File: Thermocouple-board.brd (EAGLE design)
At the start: 76.2 x 78.7 mm, 82 parts, among them J1 RJ45, J10 1X2-3.5MM, J11 1X2-3.5MM, J12 1X2-3.5MM, J13 1X2-3.5MM, J2 RJ45, J3 1981584-1, J4 2.1MMJACKTHM, J5 ST-LINK, J6 HEADER-1X3, J7 UART, SW1 PUSHBUTTON, SW2 PUSHBUTTON, U1 STM32F042K4, U10 MAX31855, U11 MAX31855, U12 MAX31855, U13 MAX31855, U20 EEPROM-I2C, U21 EEPROM-I2C, U30 ST3485, U31 ST3485, U40 LP298XS, Y1 8MHz

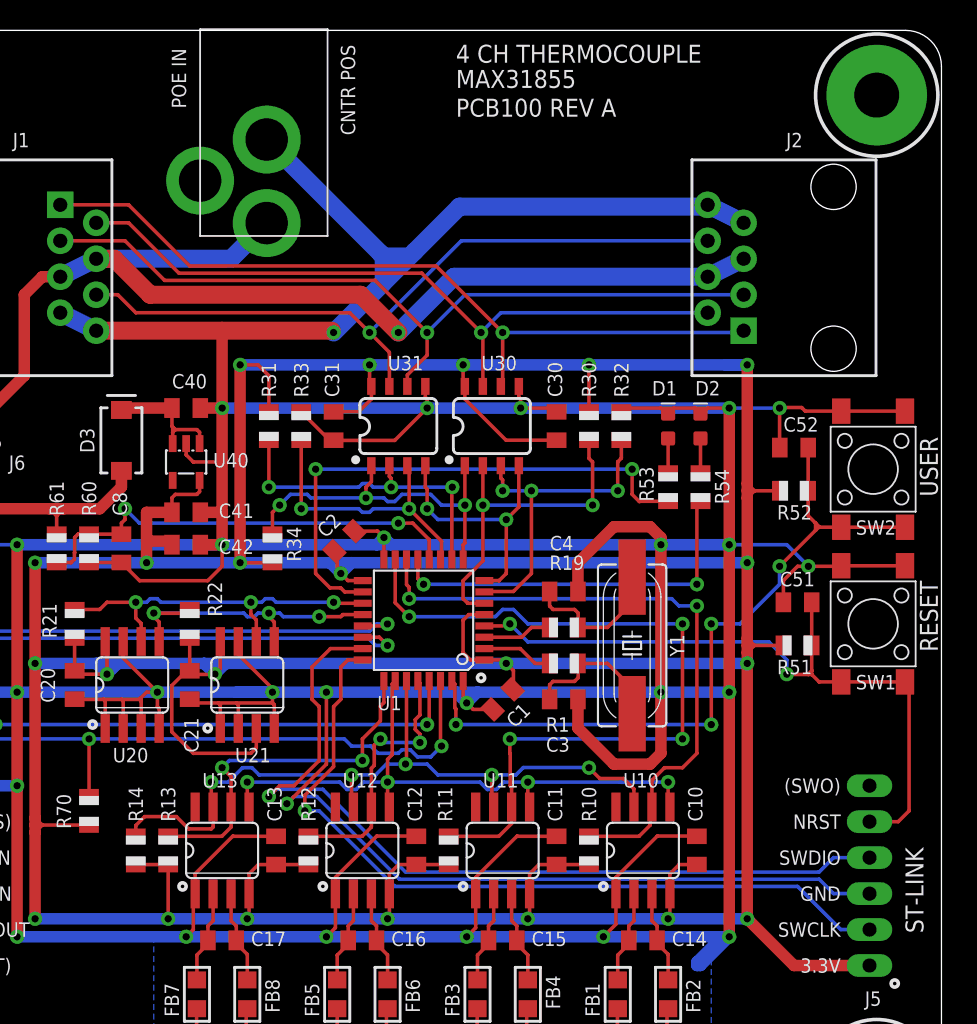
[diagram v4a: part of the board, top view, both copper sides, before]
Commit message: Fix pushbutton and SO08. Start of efuse.
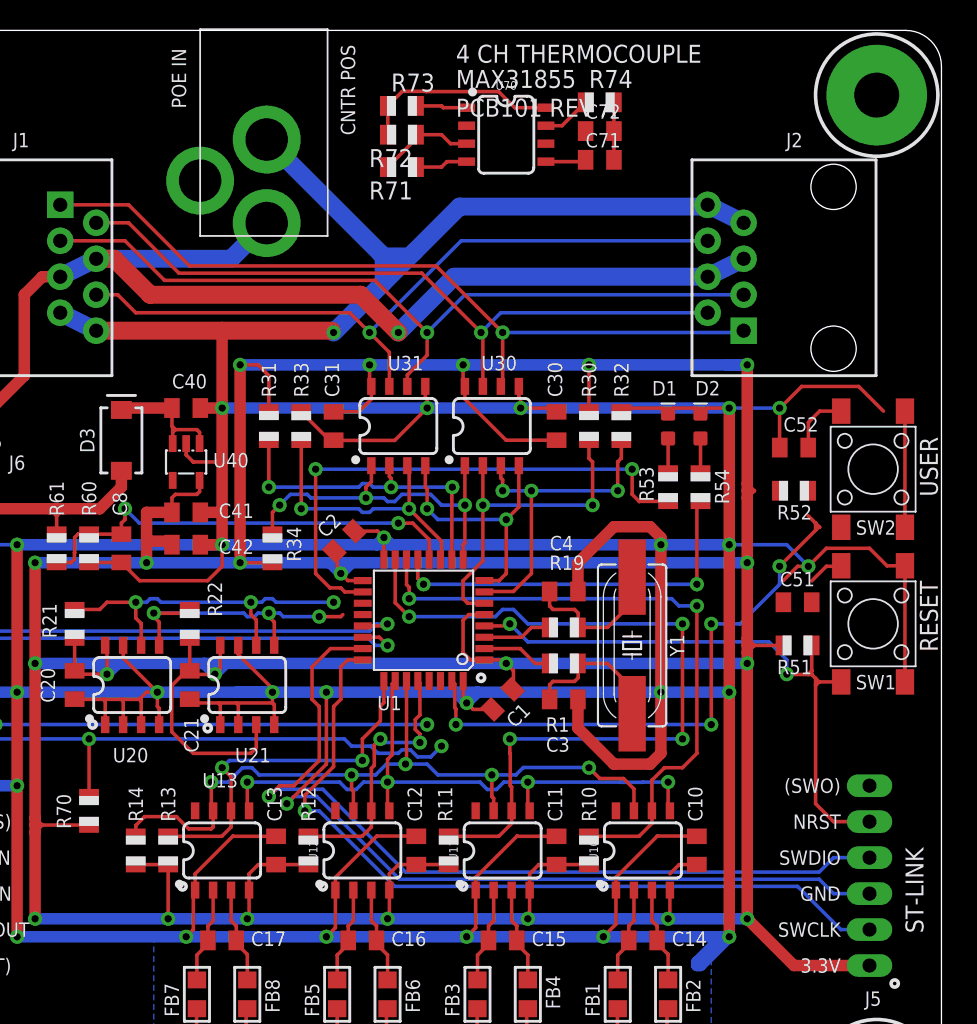
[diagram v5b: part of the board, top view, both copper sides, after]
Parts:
- added C71, C72: 10pF, adafruit:C0805K
- added R71, R72, R73, R74: 10K, adafruit:R0805
- added U70: TPS25921, Thermocouple-board:SO08
- U10, U11, U12, U13: device adafruit:SO08 -> Thermocouple-board:SO08
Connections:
- new net N$23: R71.2, R72.1, U70.3
- new net N$24: R72.2, R73.1, U70.8
- new net N$27: R74.1, U70.7
- new net N$28: C72.1, U70.2
- new net PWR_SRC: J4.TIP, R71.1, U70.4
- net +3V3: now also C52.1, SW2.1, SW2.2; no longer R52.1
- net BTN_USER: now also C52.2, R52.1, SW2.3; no longer C52.1, R52.2, SW2.2
- net GND: now also C71.2, C72.2, R52.2, R73.2, R74.2, SW1.2, U70.1; no longer C52.2, SW1.3, SW2.1, SW2.3
- net I2C_SCL: now also U1.29; no longer U1.19
- net I2C_SDA: now also U1.30; no longer U1.20
- net NRST: now also SW1.3; no longer SW1.2
- net POE_PWR: now also C71.1, U70.5; no longer J4.TIP
- net UART1_RX: now also U1.20; no longer U1.30
- net UART1_TX: now also U1.19; no longer U1.29
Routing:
- net N$24: track 0.00 -> 14.1 mm
- net GND: track 630.1 -> 642.8 mm
- net N$23: track 0.00 -> 6.94 mm
- net BTN_USER: track 52.1 -> 45.6 mm
- net +3V3: track 407.6 -> 412.8 mm
- net UART1_RX: track 55.9 -> 51.4 mm
- net NRST: track 50.0 -> 46.0 mm
- net PWR_SRC: track 0.00 -> 3.72 mm
- net N$27: track 0.00 -> 3.49 mm
- net UART1_TX: track 51.2 -> 48.3 mm
- net POE_PWR: track 82.2 -> 85.1 mm
- net I2C_SCL: track 26.9 -> 25.4 mm
- net I2C_SDA: track 22.1 -> 21.3 mm
- net SPI_MISO: track 54.1 -> 54.9 mm
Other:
- board text added: "PCB101 REV A"
- board text removed: "PCB100 REV A"

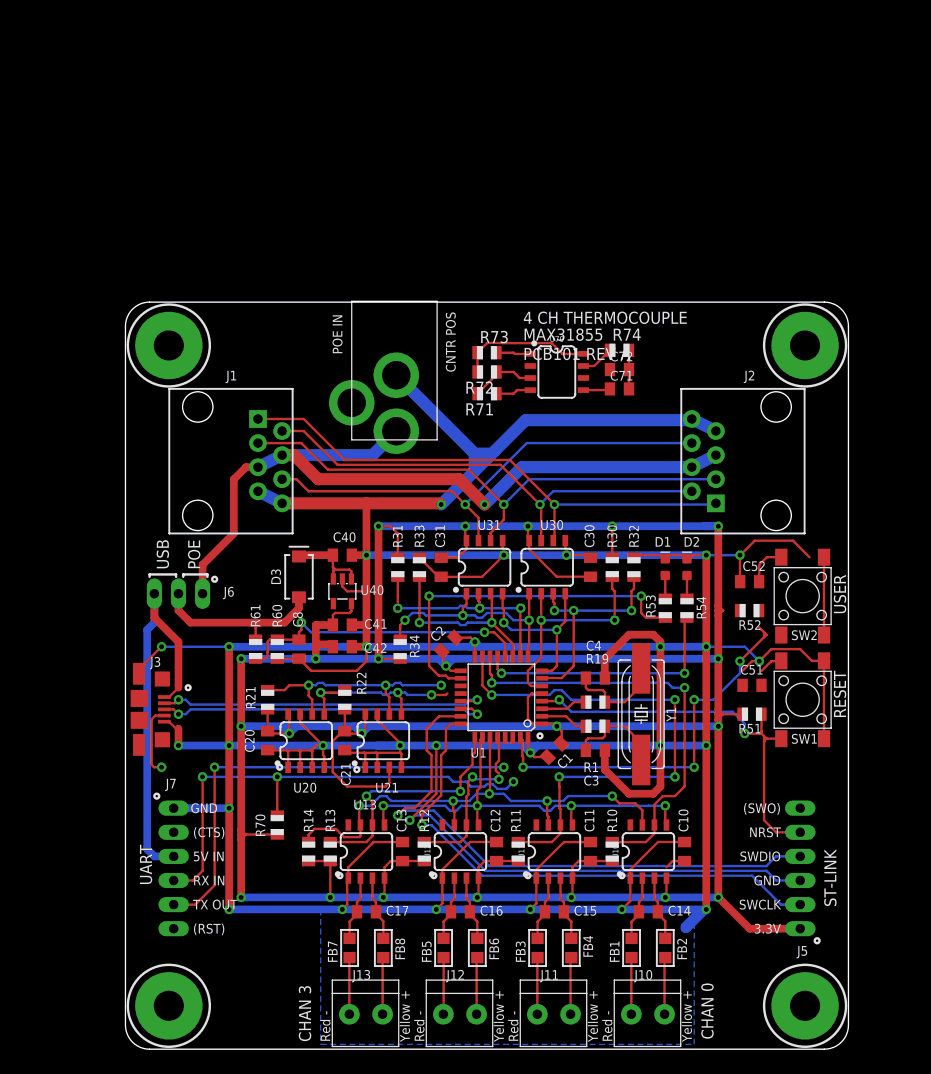
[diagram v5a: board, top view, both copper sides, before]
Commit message: RJ-45 rework routing WIP
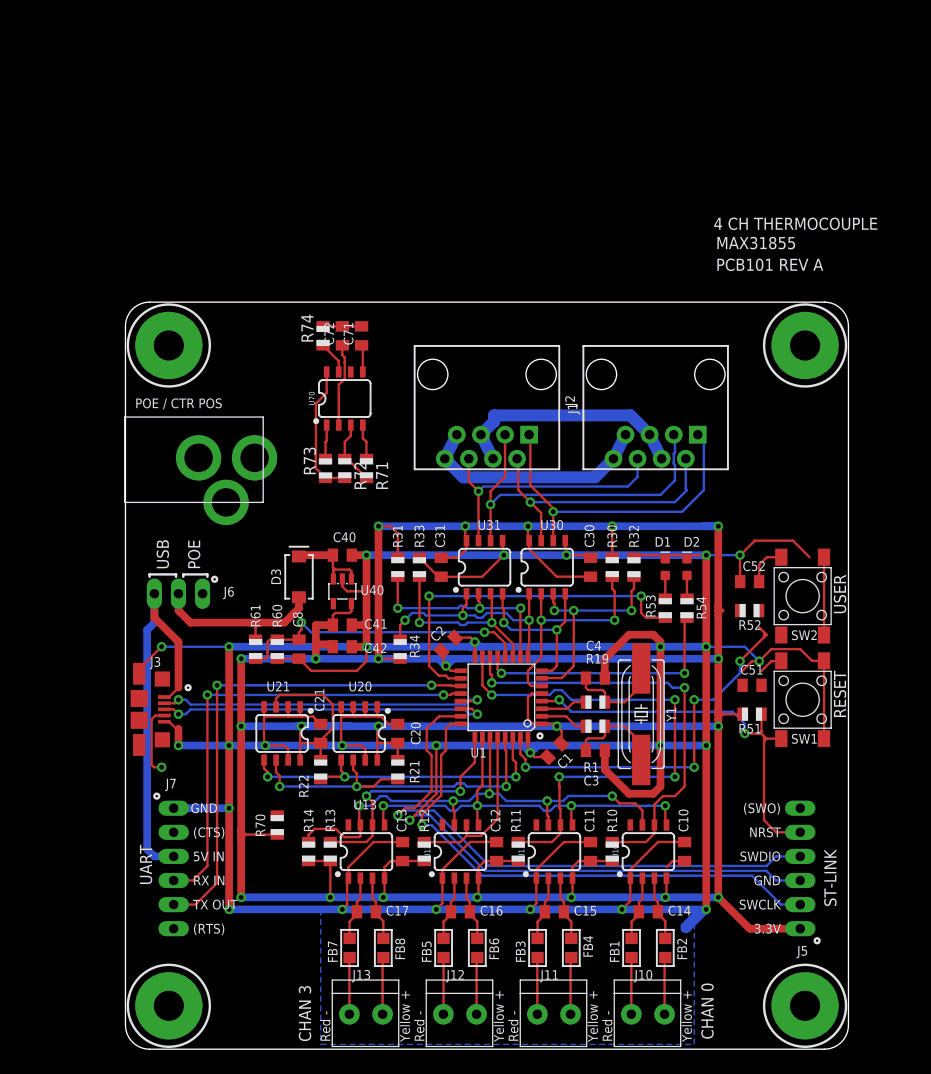
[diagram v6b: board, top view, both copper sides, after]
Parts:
- U1: value STM32F042K4 -> STM32F042K6
- moved J1 31.8 mm to (38.1, 71.1), turned to 180 degrees
- moved R74 31.3 mm to (20.8, 75.2), turned to 90 degrees
- moved C72 29.4 mm to (22.9, 75.2), turned to 90 degrees
- moved C71 27.7 mm to (24.9, 75.2), turned to 90 degrees
- moved J4 27.0 mm to (4.32, 62.2), turned to 90 degrees
- moved U70 22.5 mm to (23.1, 68.6), turned to 0 degrees
- moved R73 20.9 mm to (21.1, 61.2), turned to 90 degrees
- moved R72 18.1 mm to (23.1, 61.2), turned to 270 degrees
- moved J2 15.6 mm to (55.9, 71.1), turned to 180 degrees
- moved R21 15.6 mm to (28.7, 29.5), turned to 270 degrees
- moved R71 14.9 mm to (25.4, 61.2), turned to 270 degrees
- moved C20 13.7 mm to (28.7, 33.3), turned to 90 degrees
- moved U21 10.7 mm to (16.5, 33.3), turned to 180 degrees
- moved R22 7.79 mm to (20.6, 29.5), turned to 270 degrees
- moved U20 5.64 mm to (24.6, 33.3), turned to 180 degrees
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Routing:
- net POE_PWR: track 85.1 -> 28.4 mm, vias 1 -> 0
- net GND: track 642.8 -> 589.1 mm, vias 29 -> 28
- net UP_LINK_B: track 51.4 -> 28.4 mm
- net DN_LINK_B: track 50.9 -> 30.1 mm
- net DN_LINK_A: track 56.0 -> 35.2 mm
- net UP_LINK_A: track 56.4 -> 37.3 mm
- net I2C_SDA: track 21.3 -> 36.9 mm
- net I2C_SCL: track 25.4 -> 39.8 mm
- net N$28: track 0.00 -> 8.77 mm
- net UART1_TX: track 48.3 -> 52.1 mm
- net +3V3: track 412.8 -> 416.0 mm
- net UART1_RX: track 51.4 -> 49.0 mm, vias 3 -> 2
- net SPI_CS2_N: track 19.2 -> 18.9 mm, vias 2 -> 0
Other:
- board text added: "(RTS)"
- board text added: "POE / CTR POS"
- board text removed: "(RST)"
- board text removed: "CNTR POS"
- board text removed: "POE IN"

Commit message: Routing WIP
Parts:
- added R40, R41: 120, adafruit:R0805
- moved R52 11.8 mm to (71.4, 56.6)
- moved C51 9.94 mm to (71.4, 30.0), turned to 0 degrees
- moved R51 9.09 mm to (71.4, 27.9), turned to 180 degrees
- moved C52 7.73 mm to (71.4, 54.6)
- moved J4 2.05 mm to (4.57, 64.3)
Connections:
- net NRST renamed RST_N
- net DN_LINK_A: now also R40.2
- net DN_LINK_B: now also R40.1
- net UP_LINK_A: now also R41.2
- net UP_LINK_B: now also R41.1
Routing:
- net GND: track 589.1 -> 578.8 mm
- net RST_N: track 46.0 -> 53.8 mm
- net BTN_USER: track 45.5 -> 46.9 mm
- net POE_PWR: track 28.4 -> 29.7 mm
- net +3V3: track 416.0 -> 415.3 mm

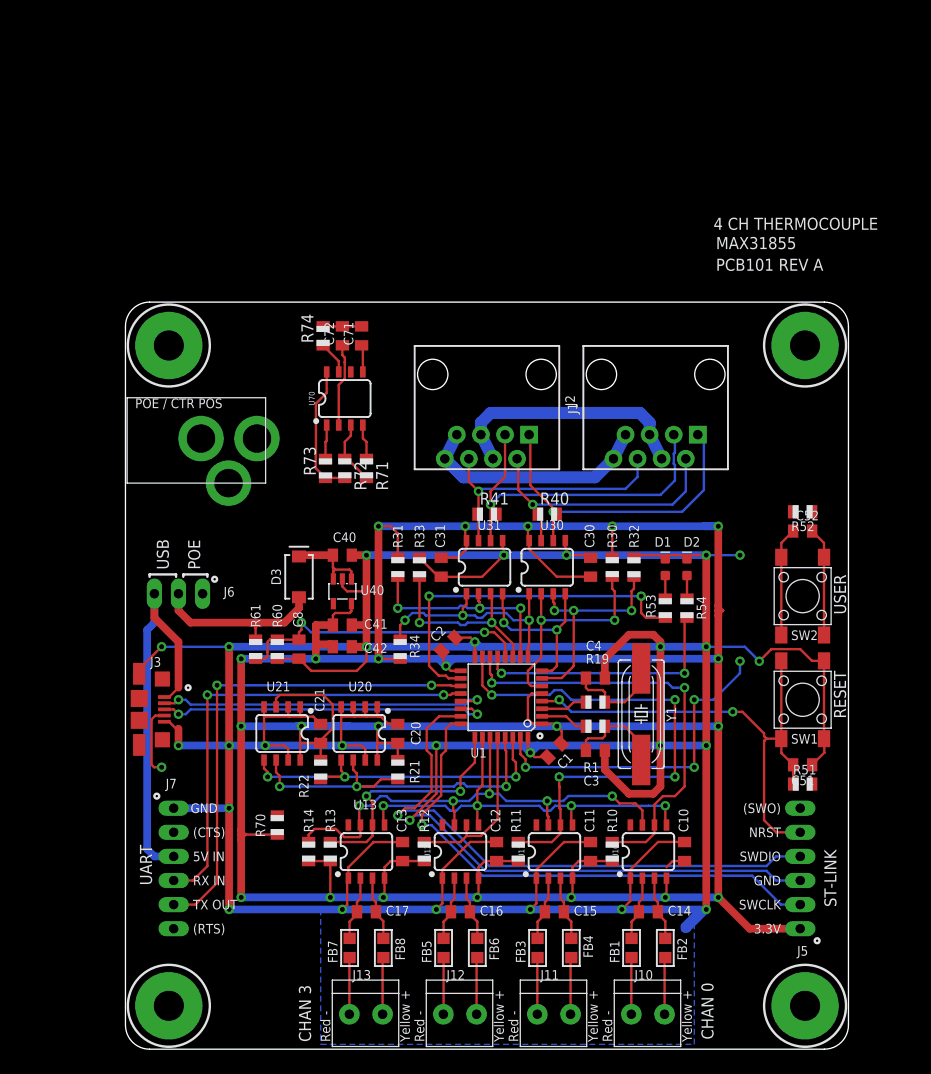
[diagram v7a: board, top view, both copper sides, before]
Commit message: Extended PCB length to 3.9 in
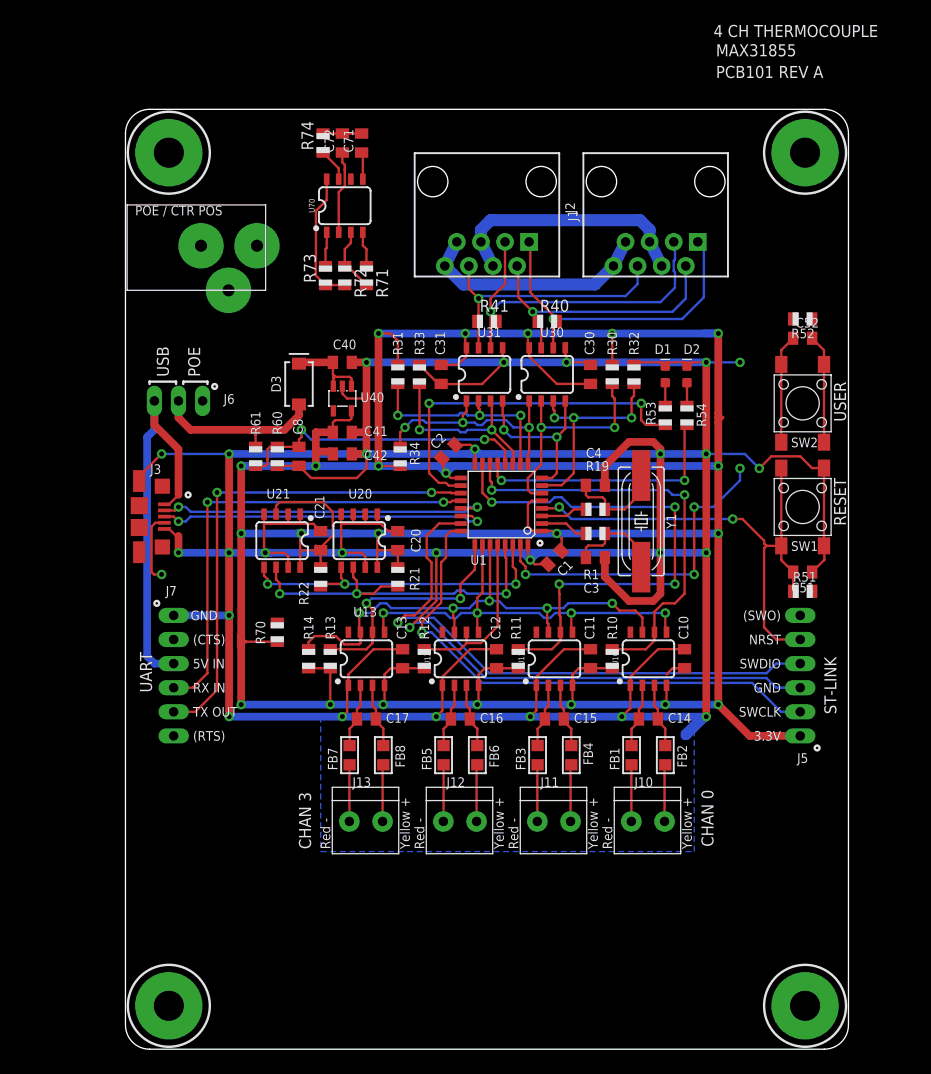
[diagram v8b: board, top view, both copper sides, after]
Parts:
- J4: device adafruit:PJ-102A -> Thermocouple-board:PJ-102A
- moved C30 20.3 mm to (49.0, 71.1)
- moved C31 20.3 mm to (33.3, 71.1)
- moved C52 20.3 mm to (71.4, 74.9)
- moved C71 20.3 mm to (24.9, 95.5)
- moved C72 20.3 mm to (22.9, 95.5)
- moved D1 20.3 mm to (56.9, 71.1)
- moved D2 20.3 mm to (59.2, 71.1)
- moved R30 20.3 mm to (51.3, 71.1)
- moved R31 20.3 mm to (28.7, 71.1)
- moved R32 20.3 mm to (53.6, 71.1)
- moved R33 20.3 mm to (31.0, 71.1)
- moved R53 20.3 mm to (56.9, 66.8)
- moved R54 20.3 mm to (59.2, 66.8)
- moved R71 20.3 mm to (25.4, 81.5)
- moved R72 20.3 mm to (23.1, 81.5)
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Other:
- board size 76.2 x 78.7 mm -> 76.2 x 99.1 mm
